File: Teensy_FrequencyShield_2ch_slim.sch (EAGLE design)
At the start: 10 parts

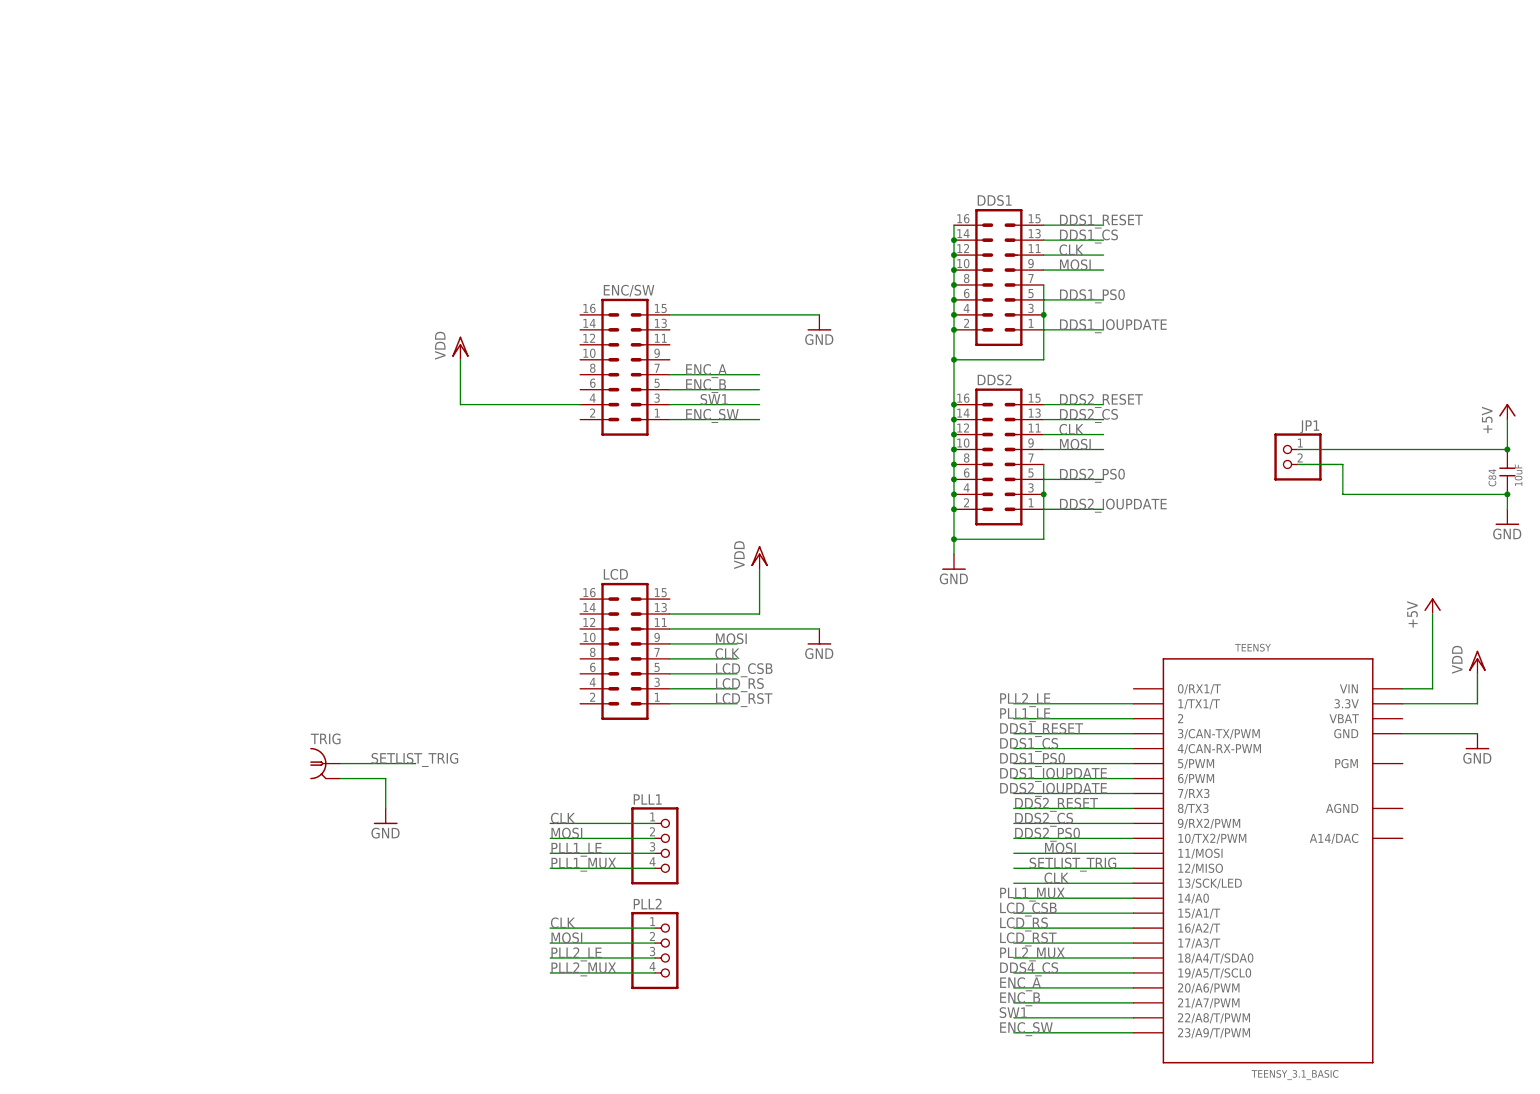
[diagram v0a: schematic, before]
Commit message: Updated 2ch teensy frequency breakout
* uses 8-pin LCD and encoder headers
* other changes possible...
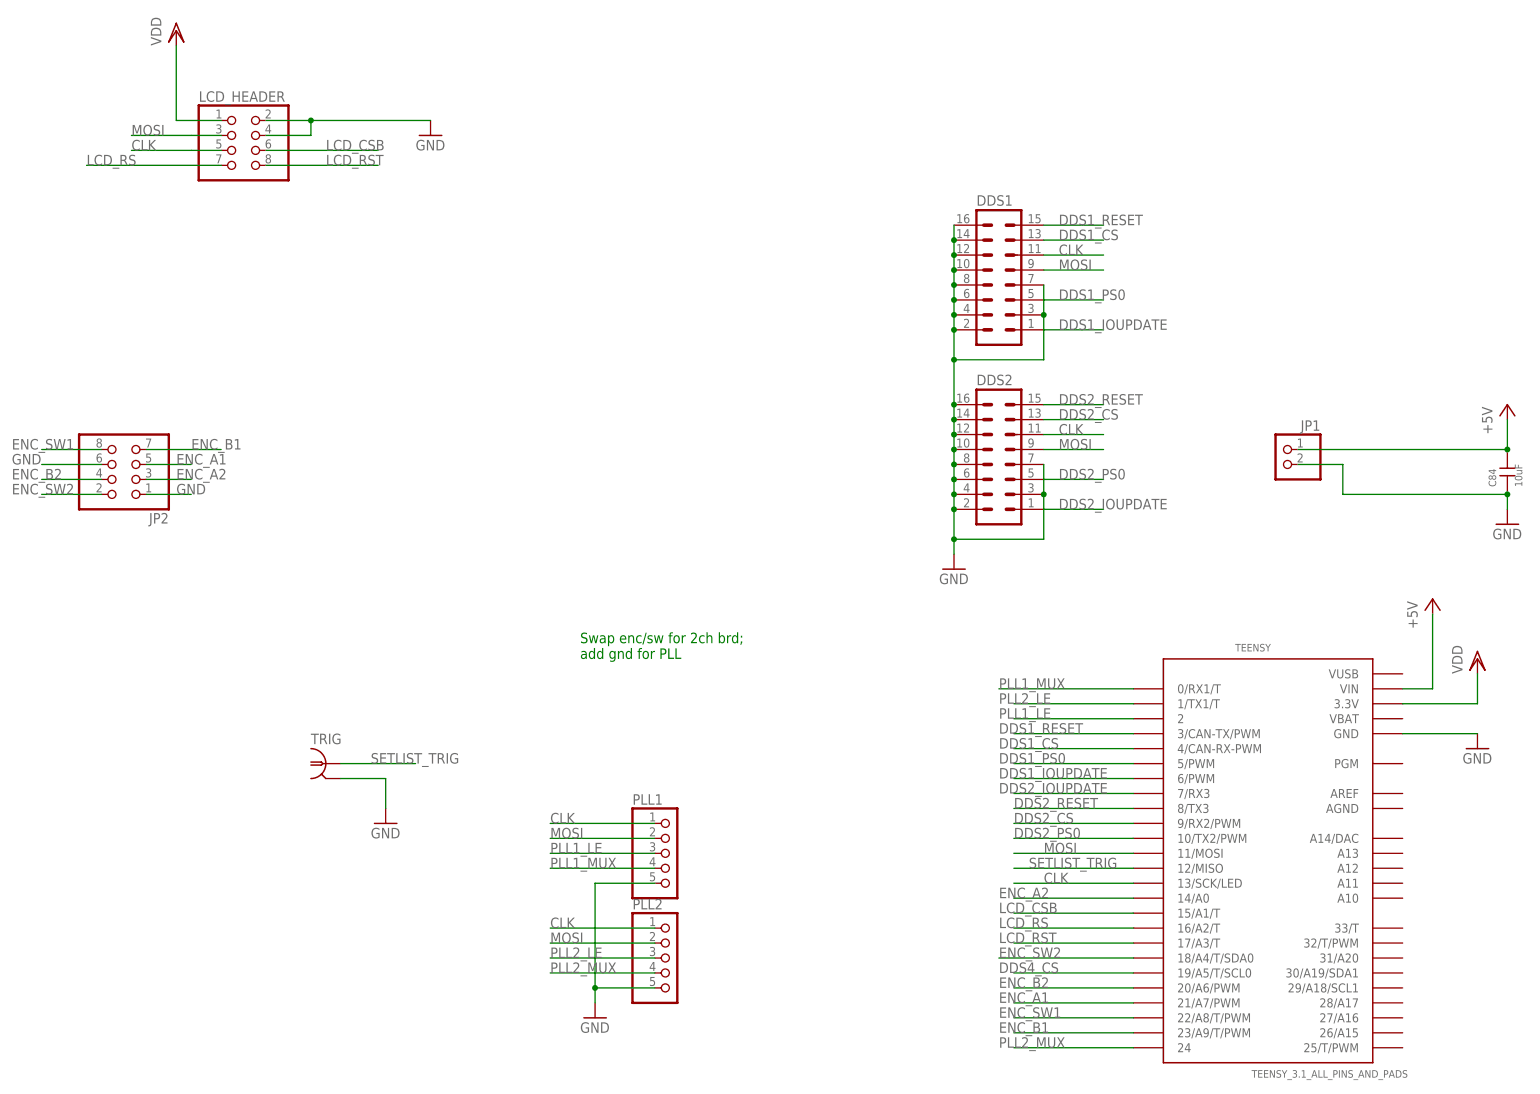
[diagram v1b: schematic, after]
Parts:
- removed ENC/SW, LCD: (no value), mcu-accessories:ML16
- added JP2, LCD_HEADER: (no value), mcu-accessories:PINHD-2X4-SHROUD
- PLL1, PLL2: device pinhead:PINHD-1X4 -> pinhead:PINHD-1X5
- TEENSY: value TEENSY_3.1_BASIC -> TEENSY_3.1_ALL_PINS_AND_PADS; device mcu-accessories:TEENSY_3.1_BASIC -> mcu-accessories:TEENSY_3.1_ALL_PINS_AND_PADS
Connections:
- removed net ENC_A: ENC/SW.7, TEENSY.20/A6/PWM
- removed net ENC_B: ENC/SW.5, TEENSY.21/A7/PWM
- removed net ENC_SW: ENC/SW.1, TEENSY.23/A9/T/PWM
- removed net SW1: ENC/SW.3, TEENSY.22/A8/T/PWM
- removed net VDD: ENC/SW.4, LCD.13, TEENSY.3.3V
- new net ENC_A1: JP2.5, TEENSY.21/A7/PWM
- new net ENC_A2: JP2.3, TEENSY.14/A0
- new net ENC_B1: JP2.7, TEENSY.23/A9/T/PWM
- new net ENC_B2: JP2.4, TEENSY.20/A6/PWM
- new net ENC_SW1: JP2.8, TEENSY.22/A8/T/PWM
- new net ENC_SW2: JP2.2, TEENSY.18/A4/T/SDA0
- new net EROU: LCD_HEADER.1, TEENSY.3.3V
- net CLK: now also LCD_HEADER.5; no longer LCD.7
- net GND: now also JP2.1, JP2.6, LCD_HEADER.2, LCD_HEADER.4, PLL1.5, PLL2.5; no longer ENC/SW.15, LCD.11
- net LCD_CSB: now also LCD_HEADER.6; no longer LCD.5
- net LCD_RS: now also LCD_HEADER.7; no longer LCD.3
- net LCD_RST: now also LCD_HEADER.8; no longer LCD.1
- net MOSI: now also LCD_HEADER.3; no longer LCD.9
- net PLL1_MUX: now also TEENSY.0/RX1/T; no longer TEENSY.14/A0
- net PLL2_MUX: now also TEENSY.24; no longer TEENSY.18/A4/T/SDA0
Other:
- note added: "Chip select bit"
- note added: "Register select"
- note added: "SPI bus"
- note added: "Swap enc/sw for 2ch brd; add gnd for PLL"
- note added: "reset"
